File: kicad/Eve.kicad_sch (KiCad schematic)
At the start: 16 parts

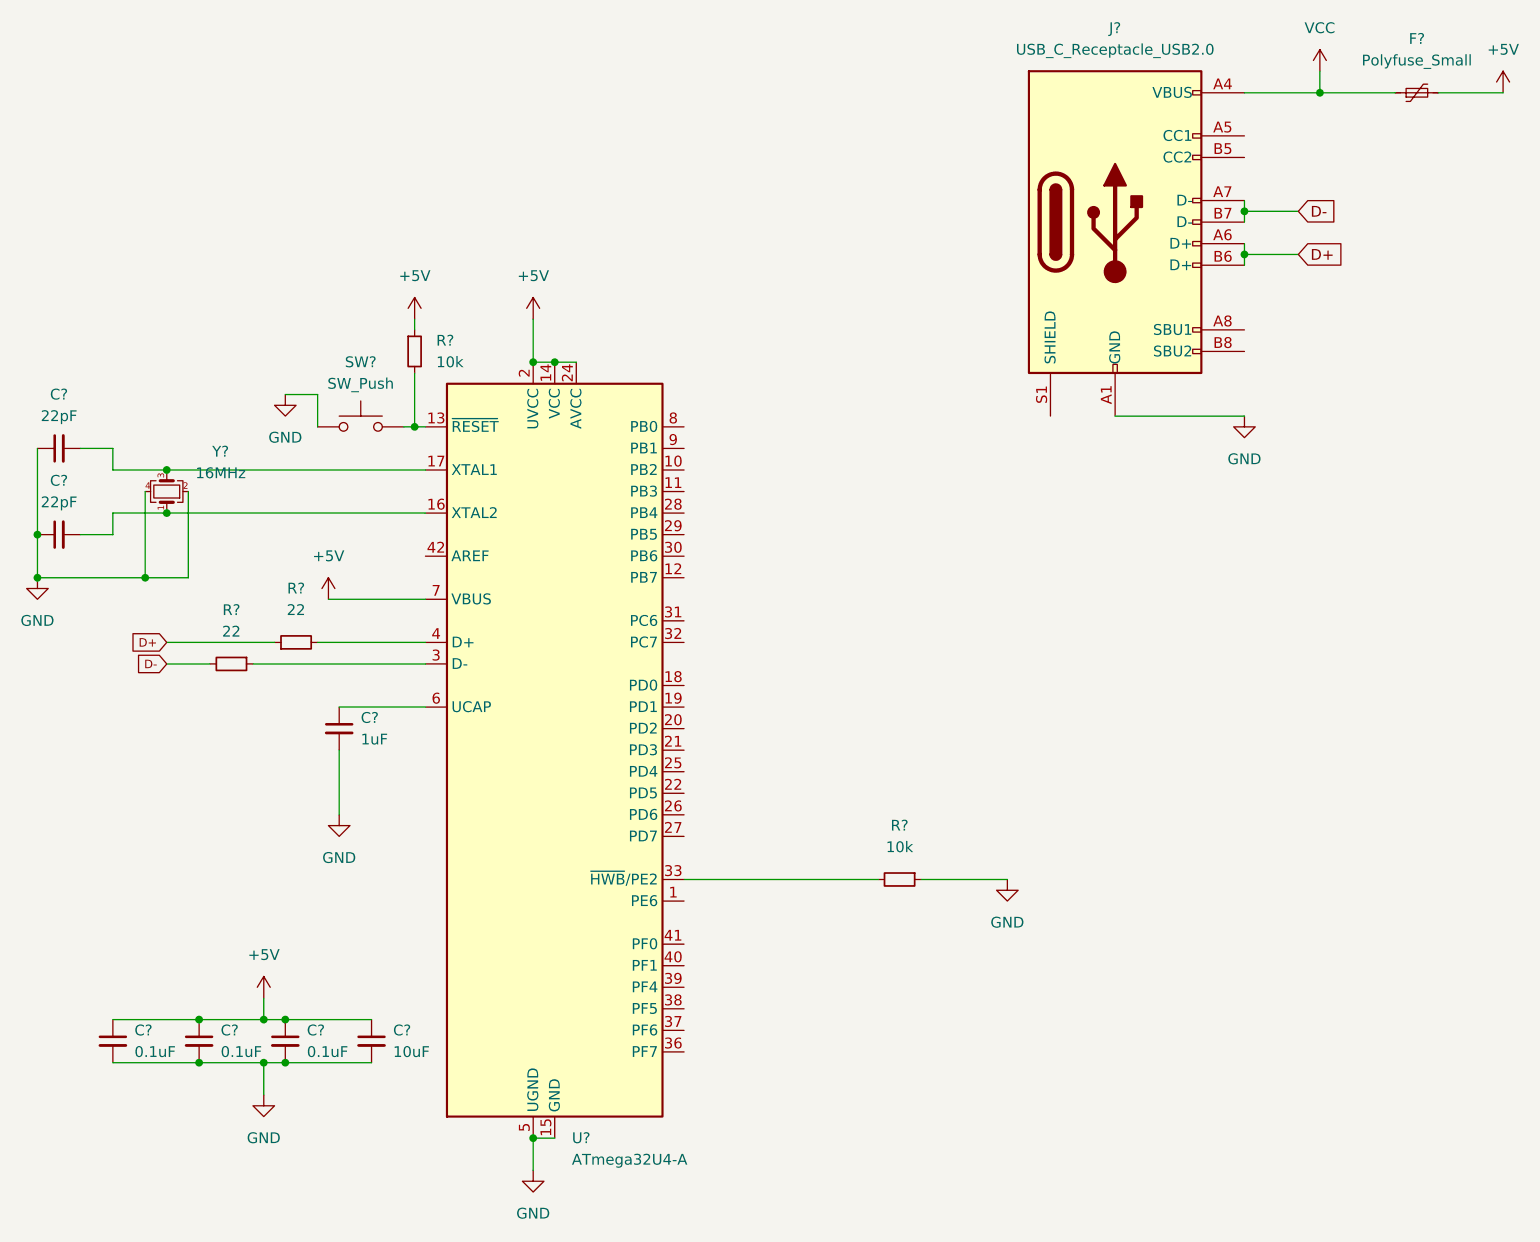
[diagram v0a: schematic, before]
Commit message: Assign footprints
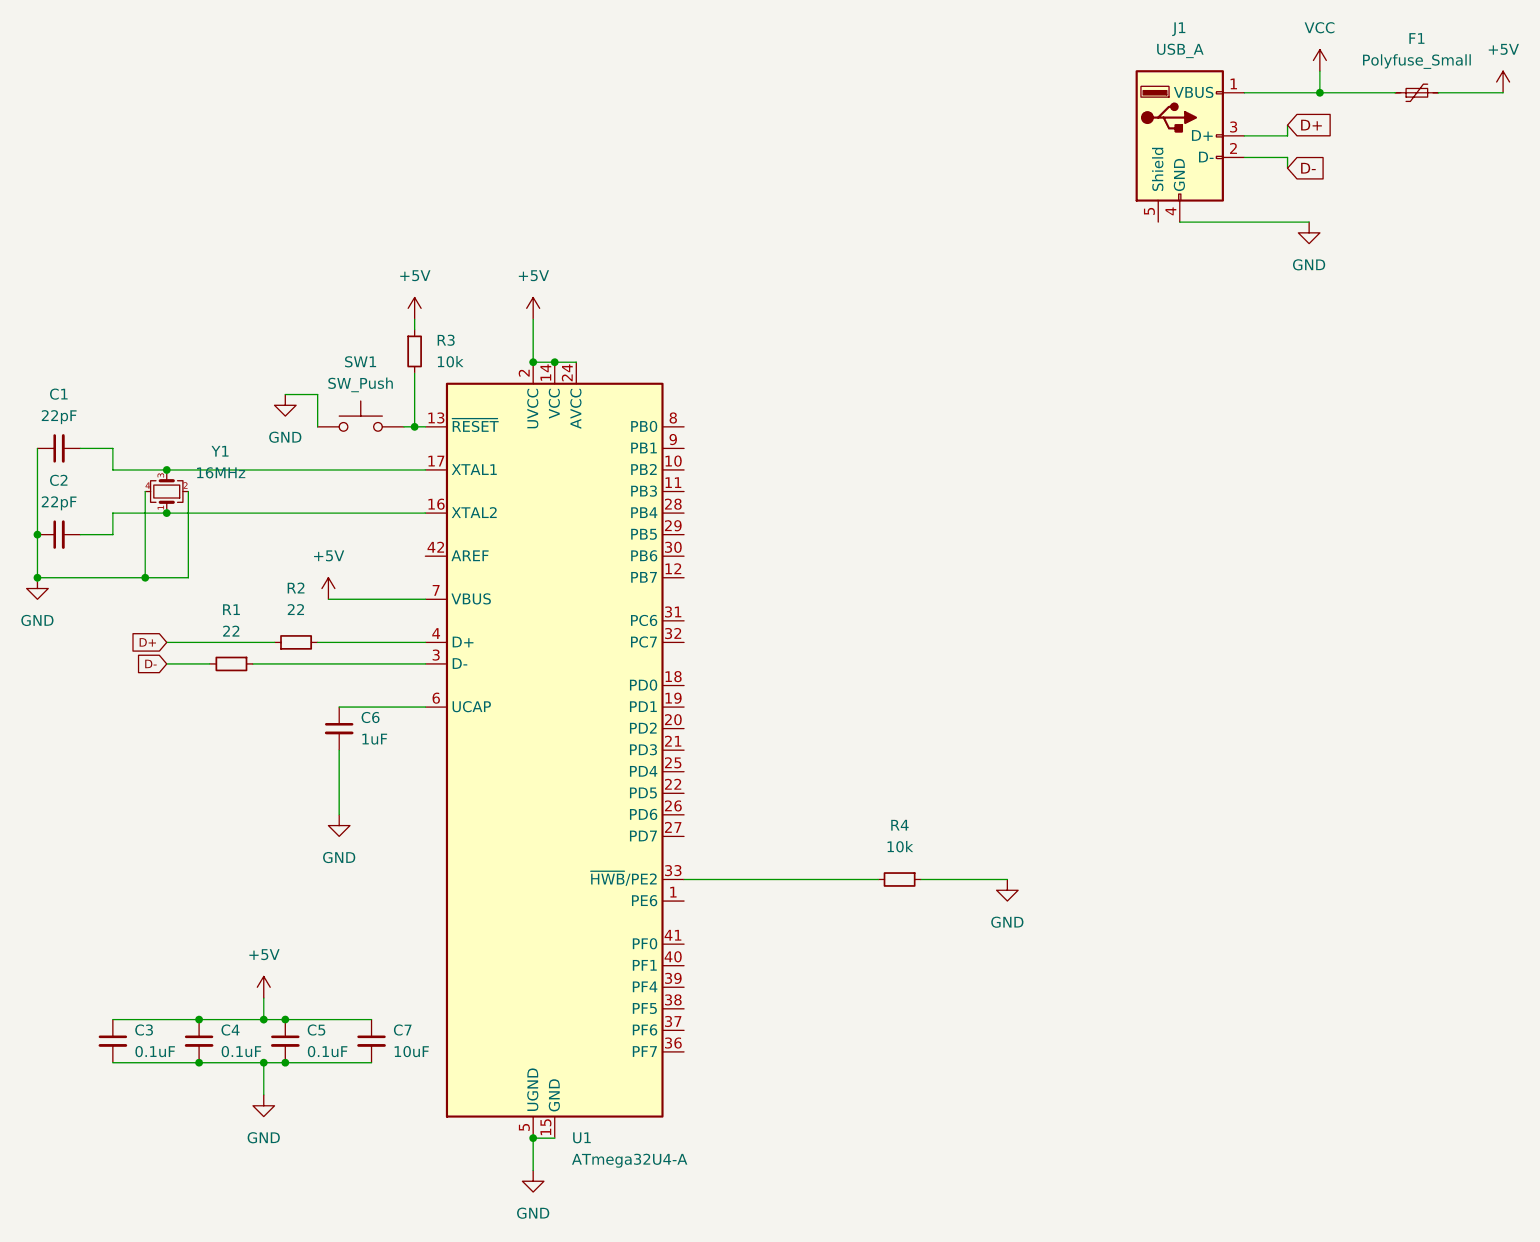
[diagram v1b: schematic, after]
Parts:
- removed J?: USB_C_Receptacle_USB2.0, symbol Connector:USB_C_Receptacle_USB2.0
- added J1: USB_A, Connector_USB:USB_Micro-B_Molex-105017-0001, symbol Connector:USB_A
- C1, C2, C3, C4, C5, C6, C7: renamed from C?; footprint (none) -> Capacitor_SMD:C_0805_2012Metric
- F1: renamed from F?; footprint (none) -> Fuse:Fuse_1206_3216Metric
- R1, R2, R3, R4: renamed from R?; footprint (none) -> Resistor_SMD:R_0805_2012Metric
- SW1: renamed from SW?; footprint (none) -> random-keyboard-parts:SKQG-1155865
- Y1: renamed from Y?; footprint (none) -> Crystal:Crystal_SMD_3225-4Pin_3.2x2.5mm
- gave numbers to parts that had none: 1
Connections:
- net D+: now also J1.3 (D+)
- net D-: now also J1.2 (D-)
- net GND: now also J1.4 (GND)
- net VCC: now also J1.1 (VBUS)
